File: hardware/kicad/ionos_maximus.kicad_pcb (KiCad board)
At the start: 2 copper layers, 45 x 39.1 mm, 49 parts, among them J1 CLH-115-F-D-DV, J2 NA(TC2030-NL), P200 TFC-120-02-F-D-A-K-TR, P201 TFC-120-02-F-D-A-K-TR, U1 LP5907MFX-3.3, U2 CAT24C32WI-GT3

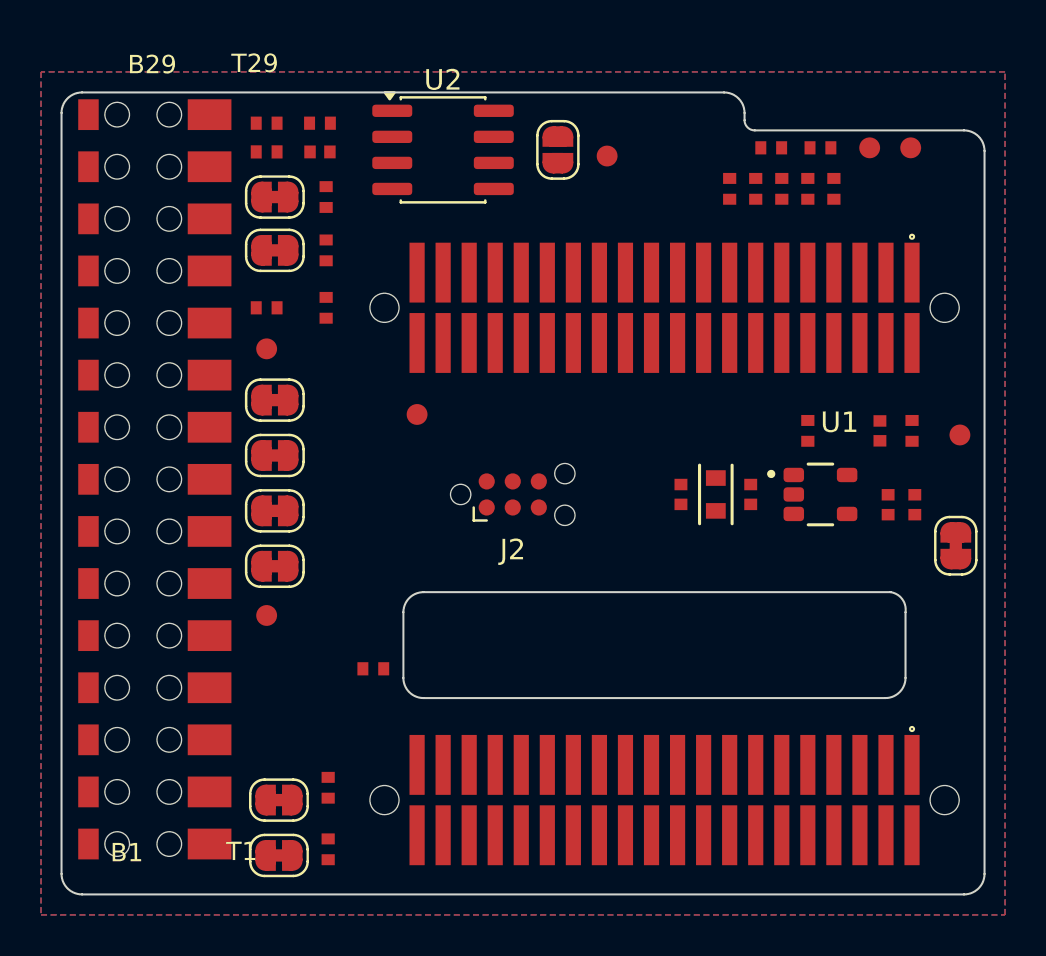
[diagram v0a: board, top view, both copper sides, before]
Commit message: hardware: rev A routed, realistic 3D renders
- Board routed on 2 layers with GND pour on both sides.
  DRC: 0 errors, 0 unconnected, schematic parity 0.
- J2 (TC2030, DNP) removed. U2 changed to TSSOP-8 and moved to
  the P200/P201 band.
- 3V3_PI taken from RPi pin 17 only. Rule-area keepout over the slot.
- gen/render_context.py: Pi 3 + radio board + SMA antenna context
  renders, built from KiCad library stand-ins.
- README images updated.

Co-Authored-By: Claude Opus 5.5 <noreply@anthropic.com>
Claude-Session: https://claude.ai/code/session_01NdGLVAcWNnBXKQpCaswFNe
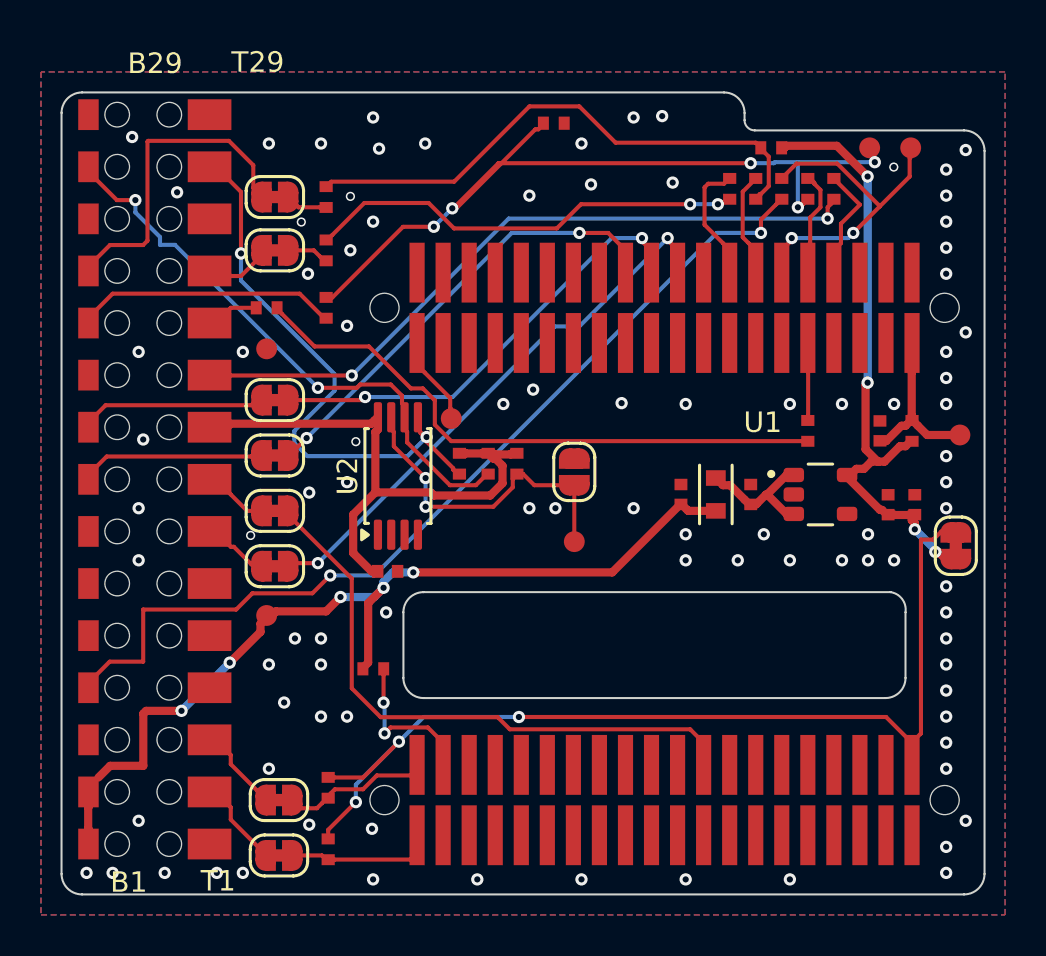
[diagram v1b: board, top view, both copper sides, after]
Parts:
- removed J2: NA(TC2030-NL), Connector:Tag-Connect_TC2030-IDC-NL_2x03_P1.27mm_Vertical
- U2: value CAT24C32WI-GT3 -> CAT24C32YI-GT3; footprint Package_SO:SOIC-8_3.9x4.9mm_P1.27mm -> Package_SO:TSSOP-8_4.4x3mm_P0.65mm
- moved C6 20.7 mm to (15.9, -15.8)
- moved R16 19.8 mm to (20.8, -21.0), turned to 90 degrees
- moved R17 19.2 mm to (22.2, -21.0), turned to 90 degrees
- moved TP3 18.9 mm to (25.0, -17.2)
- moved R15 17.9 mm to (19.4, -21.0), turned to 90 degrees
- moved U2 16.1 mm to (16.4, -20.4), turned to 90 degrees
- moved JP8 15.7 mm to (25.0, -20.6)
- moved R12 13.1 mm to (24.0, -37.6)
- moved TP6 1.68 mm to (19.0, -23.2)
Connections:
- net Net-(JP2-B) renamed /IQ_SCLK_PI
- net Net-(JP3-B) renamed /IQ_CS_PI
- net Net-(P201-Pad40) renamed /VRF_IN
- net Net-(R10-Pad2) renamed /DRDY
- net Net-(R3-Pad2) renamed /IQ_SCLK
- net Net-(R5-Pad2) renamed /IQ_CS
- net Net-(R8-Pad2) renamed /IQ_DATA
- J1 pad 2: 3V3_PI -> unconnected-(J1-3V3_[1]-Pad2)
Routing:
- net 3V3_RB: track 0.00 -> 50.5 mm, vias 0 -> 3
- net CMD_PI: track 0.00 -> 45.7 mm, vias 0 -> 2
- net 5V0: track 0.00 -> 44.6 mm, vias 0 -> 5
- net /DRDY: track 0.00 -> 39.3 mm, vias 0 -> 5
- net IQ_MOSI_PI: track 0.00 -> 34.4 mm, vias 0 -> 2
- net 3V3_RADIO: track 0.00 -> 30.6 mm, vias 0 -> 4
- net /IQ_DATA: track 0.00 -> 29.3 mm
- net RESETn_RB: track 0.00 -> 29.3 mm
- net 3V3_PI: track 0.00 -> 28.3 mm
- net ID_SC: track 0.00 -> 28.2 mm, vias 0 -> 2
- net ID_SD: track 0.00 -> 27.9 mm, vias 0 -> 2
- net SWO_RB: track 0.00 -> 27.0 mm, vias 0 -> 2
- net /IQ_CS: track 0.00 -> 26.6 mm
- net SWDIO_RB: track 0.00 -> 22.4 mm, vias 0 -> 2
- net SWCLK_RB: track 0.00 -> 22.4 mm, vias 0 -> 2
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
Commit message: hardware: JLCPCB fabrication + assembly files, DFM clean-up, final renders
- kicad/jlc/: Gerber zip, BOM (one line per LCSC code), CPL, full BOM,
  not-assembled list, part table. 26 top-side parts, 12 BOM lines.
  Every LCSC code was checked on jlcpcb.com / lcsc.com.
- CPL rotation and centre come from fitting JLC's footprint of each part
  onto the pads. P200/P201 (TFM-120, no EasyEDA model) keep KiCad's origin.
- J1 CLH-115 is not stocked at LCSC: use JLC Global Sourcing or hand-solder.
- Board DFM changes for JLC rules:
  - 9 vias moved off SMD pads (ring to pad >= 0.15 mm);
  - silkscreen cleared from via holes;
  - off-board J1 pin labels moved to Fab.
  - Result: DRC 0 errors, 0 unconnected, parity 0.
- Renders updated.

Co-Authored-By: Claude Opus 5.5 <noreply@anthropic.com>
Claude-Session: https://claude.ai/code/session_01NdGLVAcWNnBXKQpCaswFNe
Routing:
- net 3V3_RADIO: track 30.6 -> 32.3 mm
- net /DRDY: track 39.3 -> 40.6 mm
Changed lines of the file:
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@@
 		(descr "Small Outline Transistor (SOT23), 0.95 mm pitch; 5 pin, 2.95 mm L X 1.60 mm W X 1.45 mm H body\\n\\nPCB Libraries Packages")
 		(property "Reference" "U1"
-			(at -3.75 -2.925001 0)
+			(at -4.25 -2.925001 0)
 			(unlocked yes)
 			(layer "F.SilkS")
@@
 		(duplicate_pad_numbers_are_jumpers no)
 		(fp_text user "B1"
-			(at -17.66 -1.64 180)
-			(layer "F.SilkS")
+			(at -18.66 -1.64 180)
+			(layer "F.Fab")
 			(effects
 				(font
@@
 		(fp_text user "B29"
 			(at 22.26 -0.795 180)
-			(layer "F.SilkS")
+			(layer "F.Fab")
 			(effects
 				(font
@@
 		)
 		(fp_text user "T1"
-			(at -17.6 2.77 180)
-			(layer "F.SilkS")
+			(at -18.6 2.77 180)
+			(layer "F.Fab")
 			(effects
 				(font
@@
 		(fp_text user "T29"
 			(at 22.32 4.265 180)
-			(layer "F.SilkS")
+			(layer "F.Fab")
 			(effects
 				(font
@@
 		)
 		(fp_arc
-			(start -1.4 -0.3)
-			(mid -1.194975 -0.794975)
-			(end -0.7 -1)
-			(stroke
-				(width 0.15)
-				(type solid)
-			)
-			(layer "F.SilkS")
-		)
-		(fp_arc
 			(start 1.4 0.3)
 			(mid 1.194975 0.794975)
@@
 			(layer "F.CrtYd")
 		)
+		(fp_arc
+			(start -1.4 -0.3)
+			(mid -1.194975 -0.794975)
+			(end -0.7 -1)
+			(stroke
+				(width 0.15)
+				(type solid)
+			)
+			(layer "F.Fab")
+		)
 		(pad "1" smd custom
 			(at -0.65 0 90)
@@
 		)
 		(fp_line
-			(start -1.4 0.3)
-			(end -1.4 -0.3)
-			(stroke
-				(width 0.15)
-				(type solid)
-			)
-			(layer "F.SilkS")
-		)
-		(fp_line
 			(start -0.7 -1)
 			(end 0.7 -1)
@@
 		)
 		(fp_arc
-			(start -0.7 1)
-			(mid -1.194975 0.794975)
-			(end -1.4 0.3)
-			(stroke
-				(width 0.15)
-				(type solid)
-			)
-			(layer "F.SilkS")
-		)
-		(fp_arc
 			(start 0.7 -1)
 			(mid 1.194975 -0.794975)
@@
 			(layer "F.CrtYd")
 		)
+		(fp_line
+			(start -1.4 0.3)
+			(end -1.4 -0.3)
+			(stroke
+				(width 0.15)
+				(type solid)
+			)
+			(layer "F.Fab")
+		)
+		(fp_arc
+			(start -0.7 1)
+			(mid -1.194975 0.794975)
+			(end -1.4 0.3)
+			(stroke
+				(width 0.15)
+				(type solid)
+			)
+			(layer "F.Fab")
+		)
 		(pad "1" smd custom
 			(at -0.65 0)
@@
 		(tags "TSSOP SO")
 		(property "Reference" "U2"
-			(at 0 -2.45 90)
+			(at 0 -1.2 90)
 			(layer "F.SilkS")
 			(effects
@@
 		)
 		(fp_line
-			(start 2.31 1.61)
-			(end -2.31 1.61)
+			(start 1.506521 1.61)
+			(end 0.17576 1.61)
 			(stroke
 				(width 0.15)
@@
 		)
 		(fp_line
+			(start -0.376631 1.61)
+			(end -1.205218 1.61)
+			(stroke
+				(width 0.15)
+				(type default)
+			)
+			(layer "F.SilkS")
+		)
+		(fp_line
+			(start -1.782718 1.61)
+			(end -2.31 1.61)
+			(stroke
+				(width 0.15)
+				(type default)
+			)
+			(layer "F.SilkS")
+		)
+		(fp_line
 			(start -2.31 1.61)
 			(end -2.31 1.435)
@@
 		)
 		(fp_arc
-			(start 0.7 -1)
-			(mid 1.194975 -0.794975)
-			(end 1.4 -0.3)
-			(stroke
-				(width 0.15)
-				(type solid)
-			)
-			(layer "F.SilkS")
-		)
-		(fp_arc
 			(start 1.4 0.3)
 			(mid 1.194975 0.794975)
@@
 			(layer "F.CrtYd")
 		)
+		(fp_arc
+			(start 0.7 -1)
+			(mid 1.194975 -0.794975)
+			(end 1.4 -0.3)
+			(stroke
+				(width 0.15)
+				(type solid)
+			)
+			(layer "F.Fab")
+		)
 		(pad "1" smd custom
 			(at -0.65 0)
@@
 		)
 		(fp_arc
-			(start -0.7 1)
-			(mid -1.194975 0.794975)
-			(end -1.4 0.3)
-			(stroke
-				(width 0.15)
-				(type solid)
-			)
-			(layer "F.SilkS")
-		)
-		(fp_arc
 			(start 0.7 -1)
 			(mid 1.194975 -0.794975)
@@
 			(layer "F.CrtYd")
 		)
+		(fp_arc
+			(start -0.7 1)
+			(mid -1.194975 0.794975)
+			(end -1.4 0.3)
+			(stroke
+				(width 0.15)
+				(type solid)
+			)
+			(layer "F.Fab")
+		)
 		(pad "1" smd custom
 			(at -0.65 0)
@@
 	(segment
 		(start 41.6 -18.1)
-		(end 41.6 -17.8)
+		(end 41.5 -17.75)
 		(width 0.4)
 		(layer "F.Cu")
@@
 	(segment
 		(start 42.75 -16.7)
-		(end 42.6 -16.7)
+		(end 42.5 -15.85)
 		(width 0.4)
 		(layer "F.Cu")
@@
 	)
 	(via
-		(at 41.6 -17.8)
+		(at 41.5 -17.75)
 		(size 0.6)
 		(drill 0.3)
@@
 	)
 	(via
-		(at 42.6 -16.7)
+		(at 42.5 -15.85)
 		(size 0.6)
 		(drill 0.3)
@@
 	(segment
 		(start 42.6 -16.8)
-		(end 42.6 -16.7)
+		(end 42.5 -15.85)
 		(width 0.4)
 		(layer "B.Cu")
@@
 	)
 	(segment
-		(start 41.6 -17.8)
+		(start 41.5 -17.75)
 		(end 42.6 -16.8)
 		(width 0.4)
@@
 	)
 	(segment
-		(start 35.9 -33.5)
+		(start 35.75 -34.4)
 		(end 35.95 -33.5)
 		(width 0.2)
@@
 	(segment
 		(start 39.65 -35.9)
-		(end 39.65 -35.7)
+		(end 40.4 -36.2)
 		(width 0.2)
 		(layer "F.Cu")
@@
 	)
 	(via
-		(at 39.65 -35.7)
+		(at 40.4 -36.2)
 		(size 0.6)
 		(drill 0.3)
@@
 	)
 	(via
-		(at 35.9 -33.5)
-		(size 0.6)
+		(at 35.75 -34.4)
+		(size 0.45)
 		(drill 0.3)
 		(layers "F.Cu" "B.Cu")
@@
 	(segment
 		(start 35.9 -35.7)
-		(end 35.9 -33.5)
+		(end 35.75 -34.4)
 		(width 0.2)
 		(layer "B.Cu")
@@
 	)
 	(segment
-		(start 39.65 -35.7)
+		(start 40.4 -36.2)
 		(end 34.775 -35.7)
 		(width 0.2)
@@
 	)
 	(segment
-		(start 17.8 -22.3)
+		(start 17.85 -22.25)
 		(end 17.8 -22.15)
 		(width 0.2)
@@
 	)
 	(via
-		(at 17.8 -22.3)
-		(size 0.6)
+		(at 17.85 -22.25)
+		(size 0.5)
 		(drill 0.3)
 		(layers "F.Cu" "B.Cu")
@@
 	)
 	(segment
-		(start 17.8 -22.3)
+		(start 17.85 -22.25)
 		(end 16.87 -21.37)
 		(width 0.2)
@@
 	(segment
 		(start 35.6 -31.9)
-		(end 35.6 -32)
+		(end 35.7 -32.2)
 		(width 0.2)
 		(layer "F.Cu")
@@
 	)
 	(via
-		(at 35.6 -32)
+		(at 35.7 -32.2)
 		(size 0.6)
 		(drill 0.3)
@@
 	(segment
 		(start 38.35 -32)
-		(end 35.6 -32)
+		(end 35.7 -32.2)
 		(width 0.2)
 		(layer "B.Cu")
@@
 	(segment
 		(start 29.55 -31.9)
-		(end 29.55 -32)
+		(end 29.45 -32.2)
 		(width 0.2)
 		(layer "F.Cu")
@@
 	)
 	(via
-		(at 29.55 -32)
+		(at 29.45 -32.2)
 		(size 0.6)
 		(drill 0.3)
@@
 	)
 	(segment
-		(start 29.55 -32)
+		(start 29.45 -32.2)
 		(end 25.24 -27.69)
 		(width 0.2)
@@
 	(segment
 		(start 28.3 -31.85)
-		(end 28.3 -32)
+		(end 28.3 -32.25)
 		(width 0.2)
 		(layer "F.Cu")
@@
 	)
 	(via
-		(at 28.3 -32)
+		(at 28.3 -32.25)
 		(size 0.6)
 		(drill 0.3)
@@
 	(segment
 		(start 26.820074 -32)
-		(end 28.3 -32)
+		(end 28.3 -32.25)
 		(width 0.2)
 		(layer "B.Cu")
@@
 	)
 	(segment
-		(start 32 -33.65)
+		(start 31.85 -33.65)
 		(end 32.1 -33.75)
 		(width 0.2)
@@
 	)
 	(via
-		(at 32 -33.65)
-		(size 0.6)
+		(at 31.85 -33.65)
+		(size 0.5)
 		(drill 0.3)
 		(layers "F.Cu" "B.Cu")
@@
 	(segment
 		(start 30.65 -33.65)
-		(end 32 -33.65)
+		(end 31.85 -33.65)
 		(width 0.2)
 		(layer "B.Cu")
